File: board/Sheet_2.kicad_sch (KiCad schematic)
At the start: 9 parts, among them Q1 AO3400A, U4 LED strip, U5 LIS2DH12TR

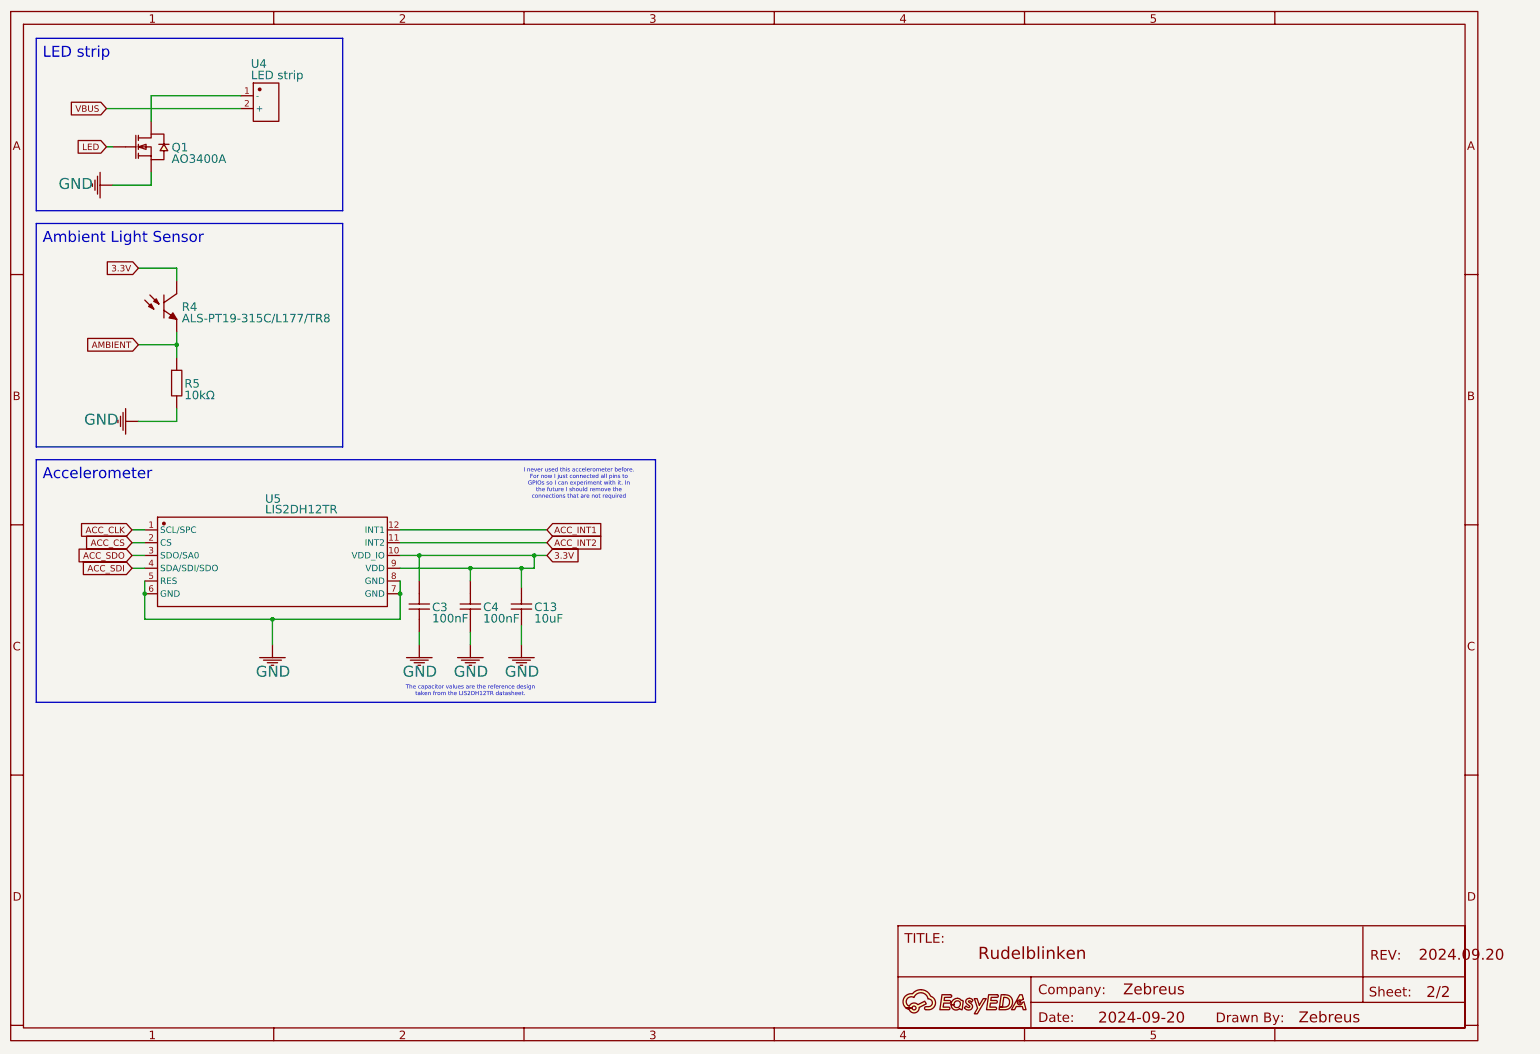
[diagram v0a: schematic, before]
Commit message: Organize schematics for kicad
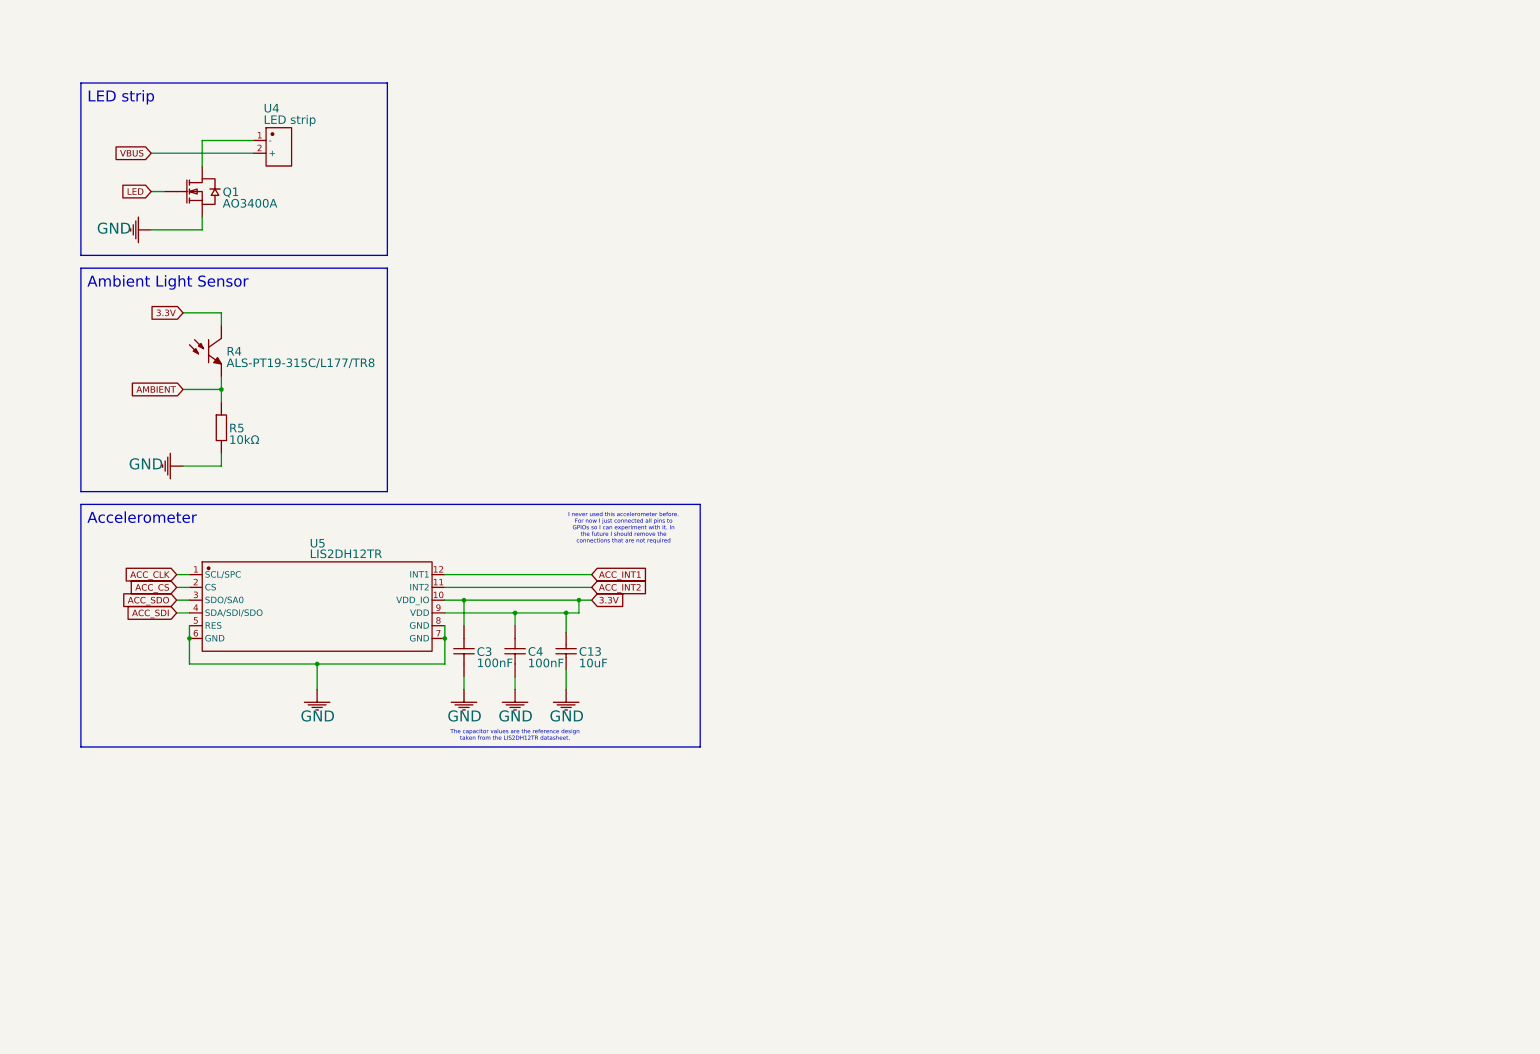
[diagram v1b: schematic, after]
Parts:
- removed A: A, symbol Unknown_0_-806
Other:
- company: (none) -> Zebreus
- title: (none) -> Rudelblinken
- moved on the sheet: C13, C3, C4, Q1, R4, R5, U4, U5
